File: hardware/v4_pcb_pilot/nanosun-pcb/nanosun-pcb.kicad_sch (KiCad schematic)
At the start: 29 parts, among them J1 Conn_01x03

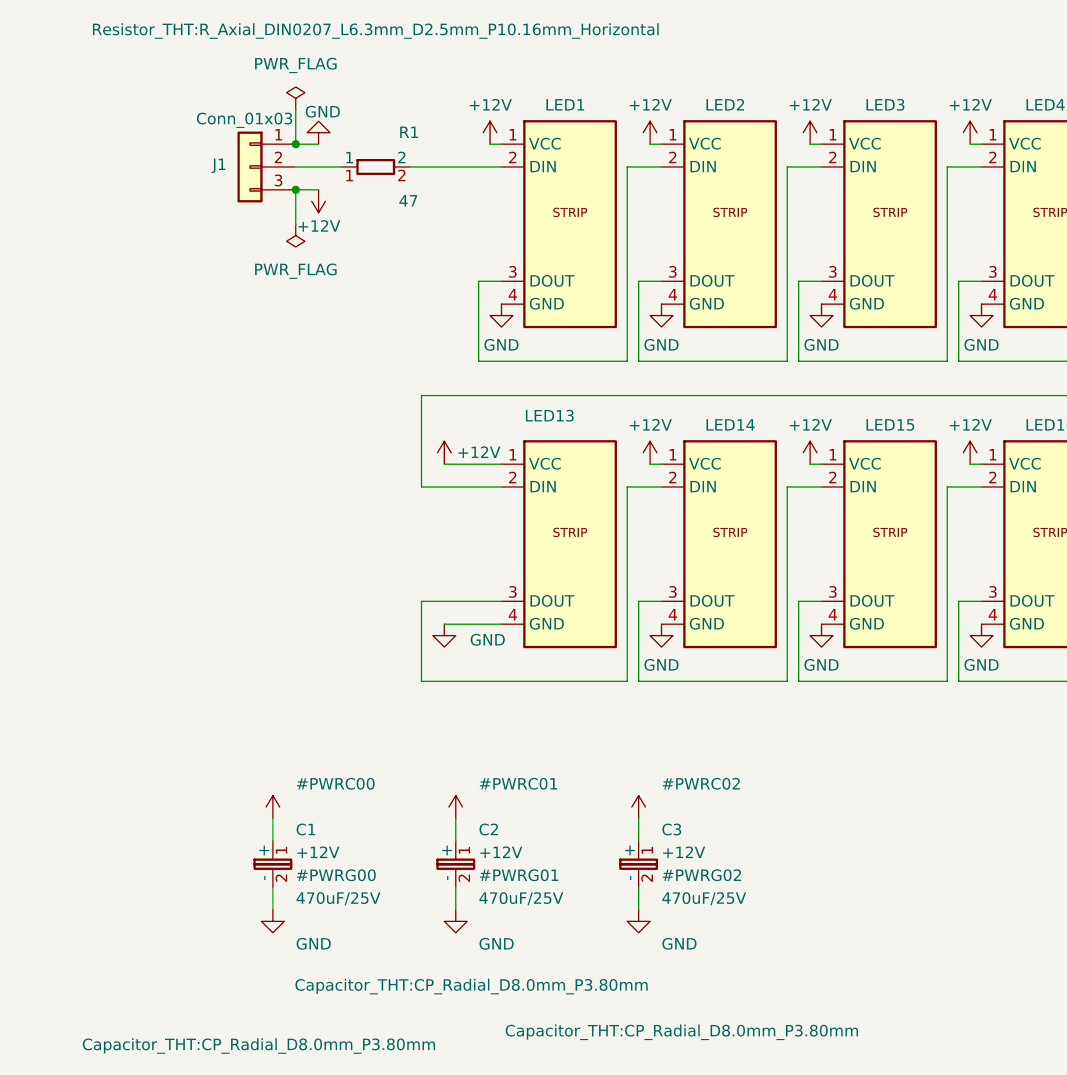
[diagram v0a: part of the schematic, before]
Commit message: circle pcb with touchups
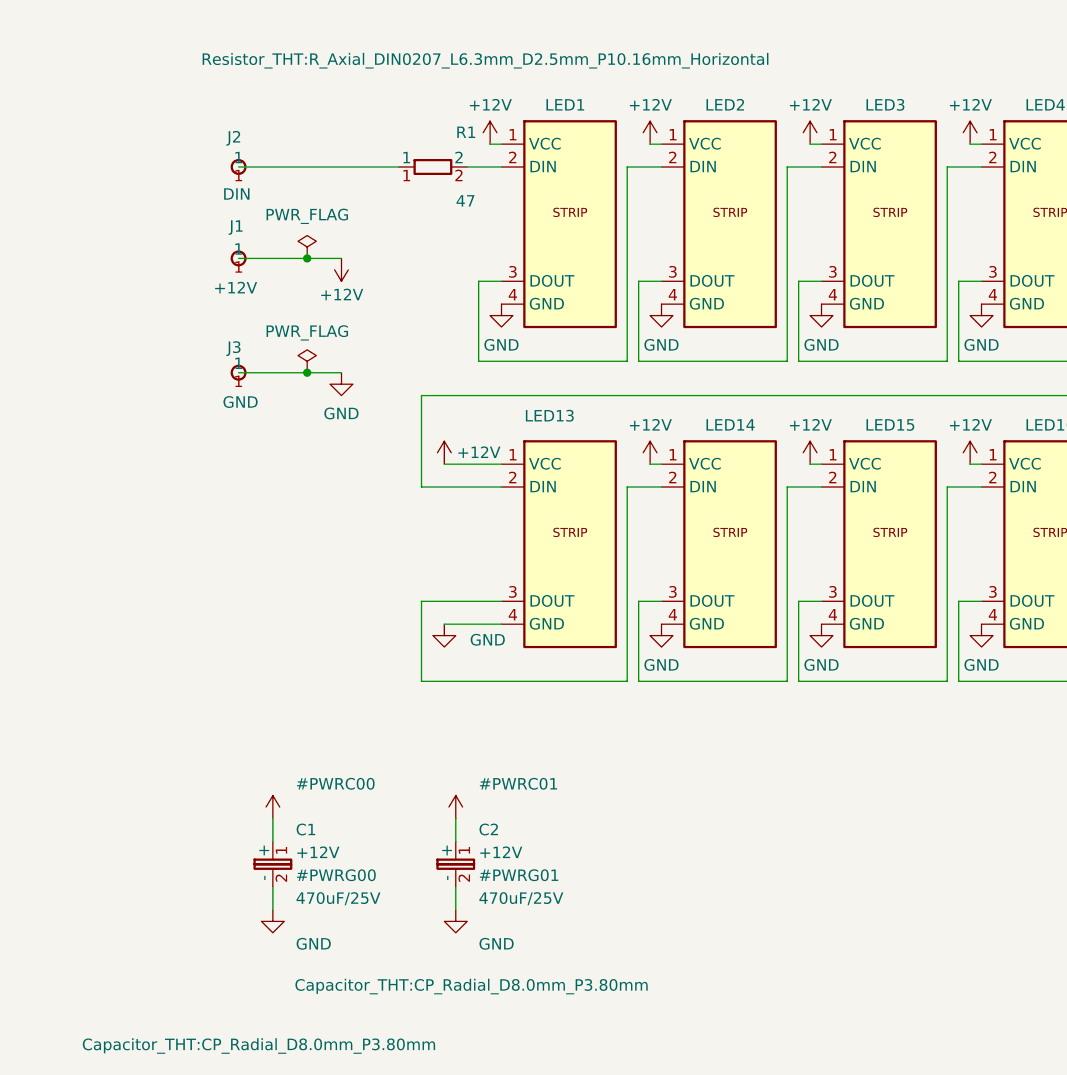
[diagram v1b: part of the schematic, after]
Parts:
- removed C3: 470uF/25V, Capacitor_THT:CP_Radial_D8.0mm_P3.80mm, symbol nanosun-pcb:CP_THT
- removed J1: Conn_01x03, TerminalBlock_Phoenix:TerminalBlock_Phoenix_MKDS-1,5-3_1x03_P5.00mm_Horizontal, symbol Connector_Generic:Conn_01x03
- added J1: +12V, nanosun-pcb:WireSolderPad_1, symbol nanosun-pcb:WireSolderPad
- added J2: DIN, nanosun-pcb:WireSolderPad_1, symbol nanosun-pcb:WireSolderPad
- added J3: GND, nanosun-pcb:WireSolderPad_1, symbol nanosun-pcb:WireSolderPad
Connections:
- net +12V: now also J1.1
- net GND: now also J3.1
- net at R1.1: now also J2.1
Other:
- moved on the sheet: R1
